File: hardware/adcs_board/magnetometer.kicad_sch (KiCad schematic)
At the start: 66 parts, among them T3 IRF7105TR, T4 IRF7105TR, U25 HMC1002-TR, U26 LM324NSR, U27 HMC1001-RC, U28 ADS1257IRGWT, U29 LM324NSR, U5 MT3608, U6 MT3608

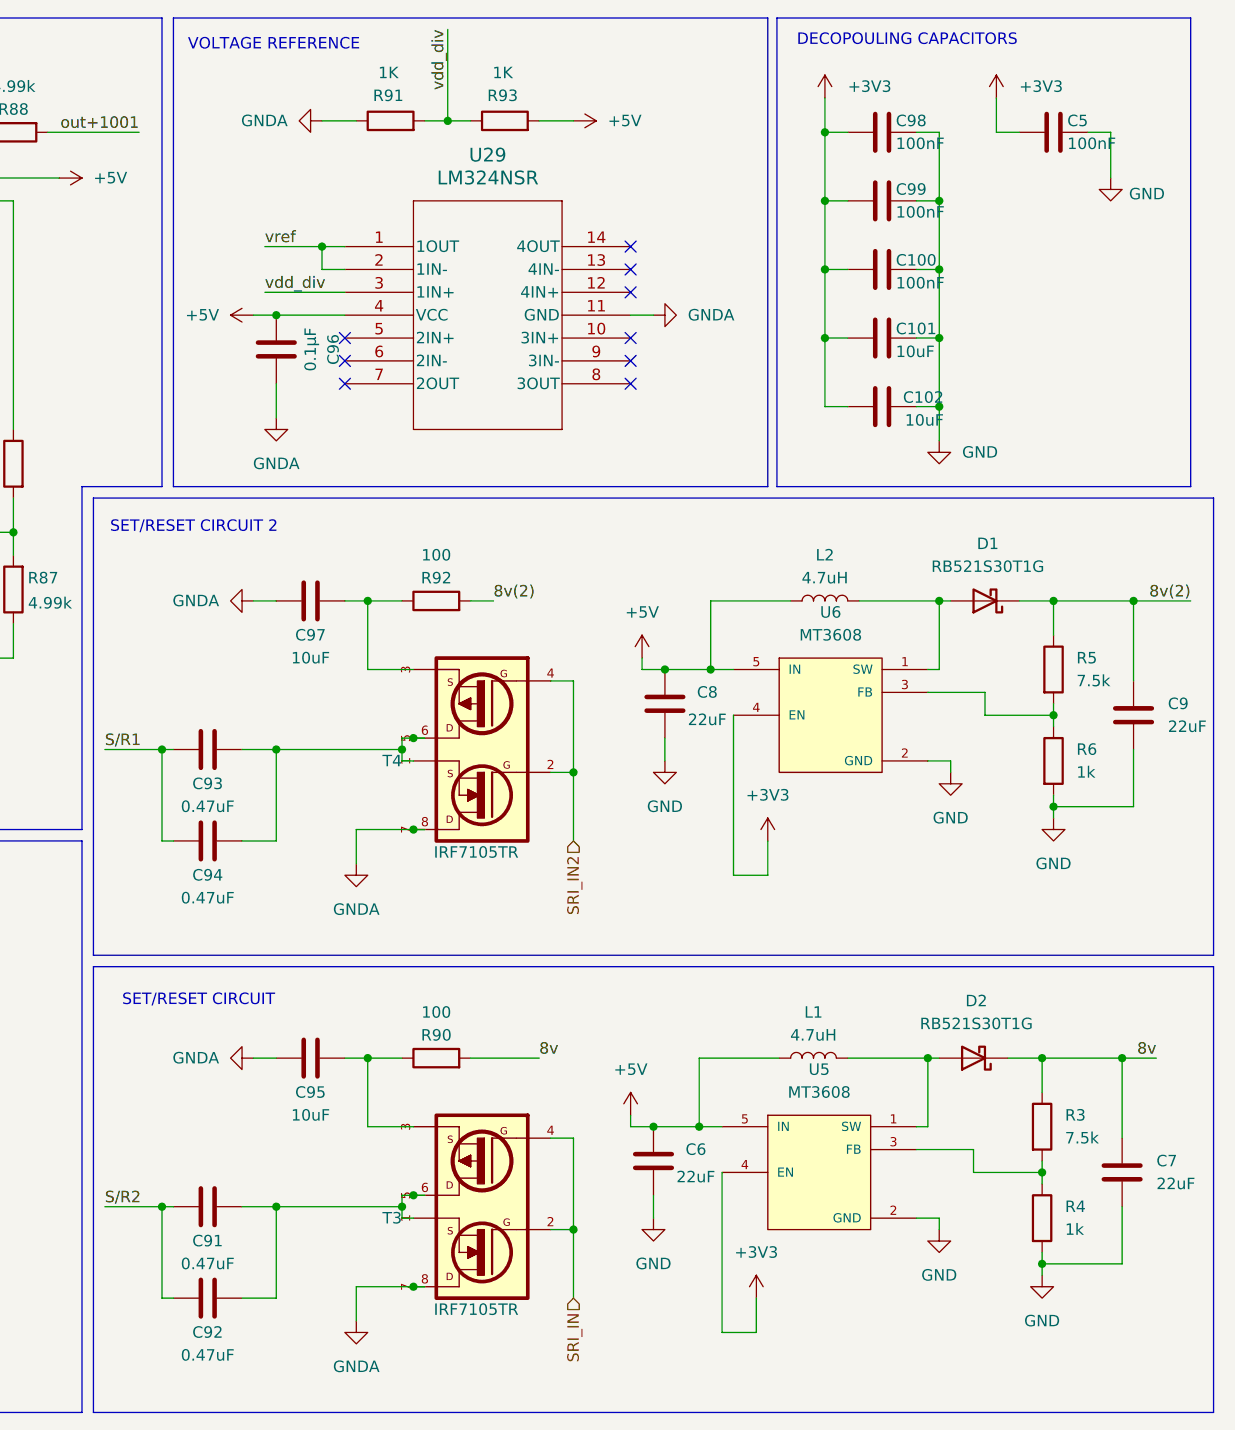
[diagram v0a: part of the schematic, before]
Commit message: Update and fix part number issues
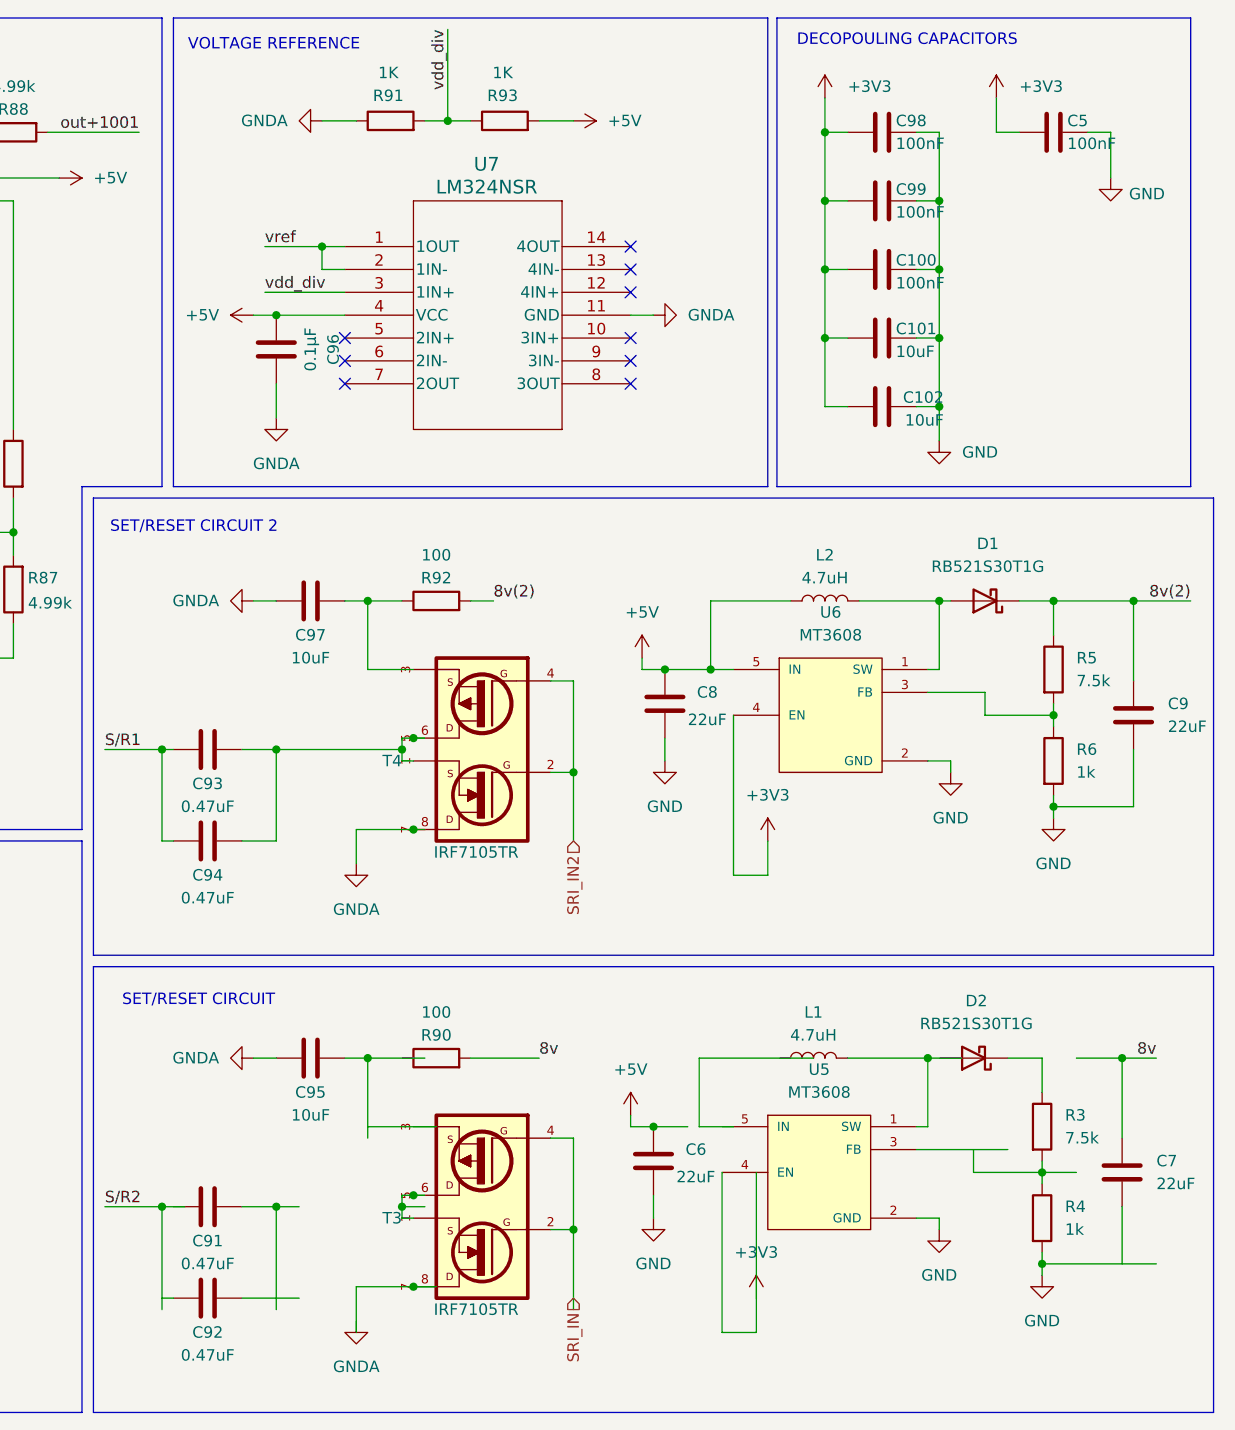
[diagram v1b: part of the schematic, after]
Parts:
- removed U29: LM324NSR, adcs_board:NS14, symbol adcs_board:LM324NSR
- added U7: LM324NSR, adcs_board:NS14, symbol adcs_board:LM324NSR
- T3, T4: Availability Not in stock -> (none); Check_prices https://www.snapeda.com/parts/IRF7105/Infineon+Technologies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 -> (none); MP IRF7105 -> (none); Package SOIC-8 International Rectifier -> (none); Price None -> (none); Purchase-URL https://www.snapeda.com/api/url_track_click_mouser/?unipart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 -> (none); SnapEDA_Link https://www.snapeda.com/parts/IRF7105/Infineon+Technologies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 -> (none)
- U25, U27: MF (none) -> Honeywell Aerospace
- U26, U28: MF (none) -> Texas Instruments
- U5: Availability Not in stock -> (none); Check_prices https://www.snapeda.com/parts/MT3608/Aerosemi+Technology+Co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 -> (none); Description_1 High Efficiency 1.2MHz 2A Step Up Converter -> (none); MANUFACTURER Aero Semi -> (none); MAXIMUM_PACKAGE_HEIGHT 1.45mm -> (none); MP MT3608 -> (none); PARTREV 1.0 -> (none); Package Package -> (none); Price None -> (none); STANDARD IPC-7351B -> (none); SnapEDA_Link https://www.snapeda.com/parts/MT3608/Aerosemi+Technology+Co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 -> (none)
- U6: Availability Not in stock -> (none); Check_prices https://www.snapeda.com/parts/MT3608/Aerosemi+Technology+Co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 -> (none); Description_1 High Efficiency 1.2MHz 2A Step Up Converter -> (none); MANUFACTURER Aero Semi -> (none); MAXIMUM_PACKAGE_HEIGHT 1.45mm -> (none); MF Aerosemi Technology Co., Ltd -> AEROSEMI; MP MT3608 -> (none); PARTREV 1.0 -> (none); Package Package -> (none); Price None -> (none); STANDARD IPC-7351B -> (none); SnapEDA_Link https://www.snapeda.com/parts/MT3608/Aerosemi+Technology+Co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 -> (none)
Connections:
- net +3V3: no longer U5.4 (EN)
- net +5V: now also U7.4 (VCC); no longer L1.1, U5.5 (IN)
- net 8v: no longer D2.1 (K), R3.1
- net GND: no longer C7.2
- net GNDA: now also U7.11 (GND); no longer T3.7, T3.8
- net S/R2: no longer C91.1, C92.1
- net vdd_div: now also U7.3 (1IN+)
- net vref: now also U7.1 (1OUT), U7.2 (1IN-)
- net at T3.1, T3.5, T3.6: no longer C91.2, C92.2
- net at L1.2, U5.1 (SW): no longer D2.2 (A)
- net at R3.2, R4.1: no longer U5.3 (FB)
- new net: D2.1 (K), R3.1
- now unconnected: C95.2, R90.1, T3.3

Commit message: hardware: schematic and layout fixes
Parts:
- renumbered C8 to C6, C9 to C7, C6 to C8, C7 to C9, L2 to L1, L1 to L2, R5 to R3, R6 to R4, R3 to R5, R4 to R6, U7 to U29
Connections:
- net +3V3: now also U5.4 (EN)
- net +5V: now also L2.1, U5.5 (IN)
- net 8v: now also D2.1 (K), R5.1
- net GND: now also C9.2
- net GNDA: now also T3.7, T3.8
- net S/R2: now also C91.1, C92.1
- net at C92.2: now also C91.2, T3.1, T3.5, T3.6
- net at L2.2, U5.1 (SW): now also D2.2 (A)
- net at R5.2, R6.1: now also U5.3 (FB)
- net at T3.3: now also C95.2, R90.1
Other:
- moved on the sheet: C100, C101, C102, C5, C6, C7, C84, C85, C86, C87, C93, C94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
